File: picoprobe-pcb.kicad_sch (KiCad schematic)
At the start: 3 parts, among them J1 Conn_01x07_Male, J2 Conn_ARM_JTAG_SWD_10, U1 Pico

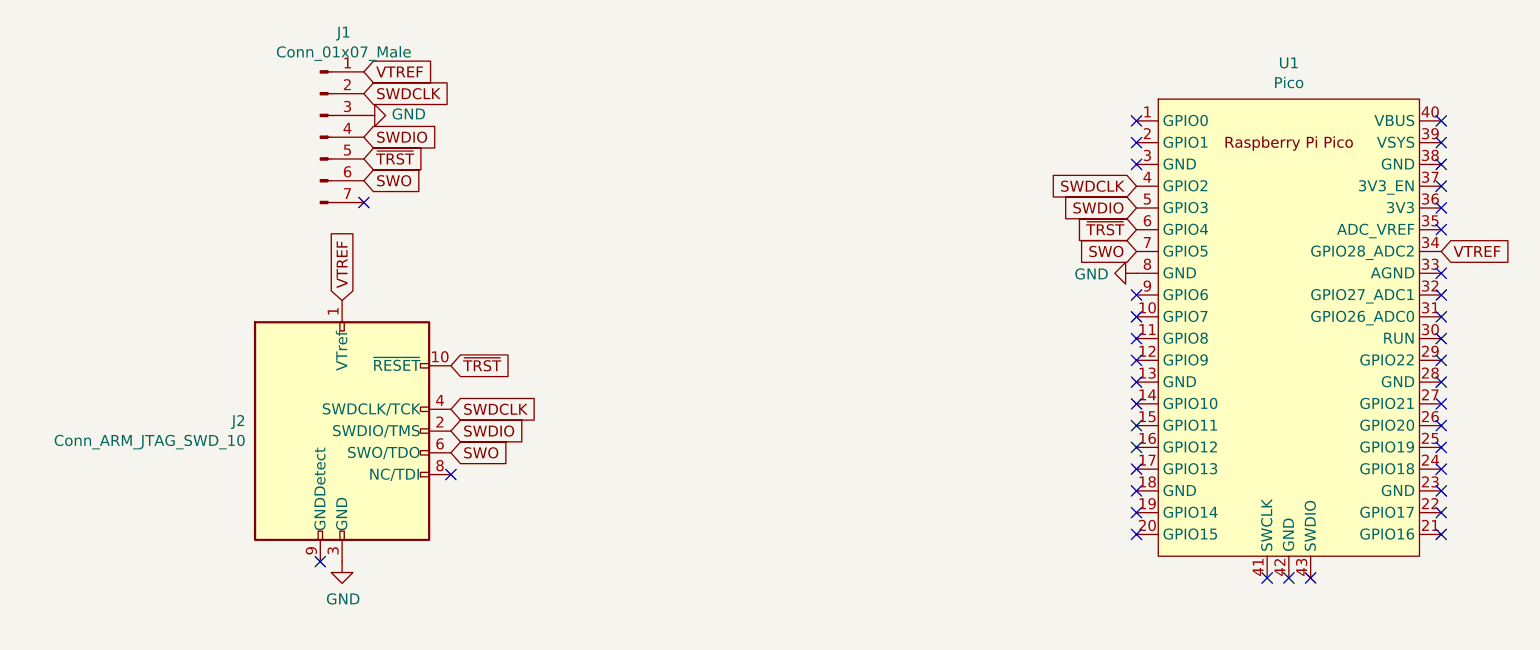
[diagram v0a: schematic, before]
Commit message: Clean up schematic
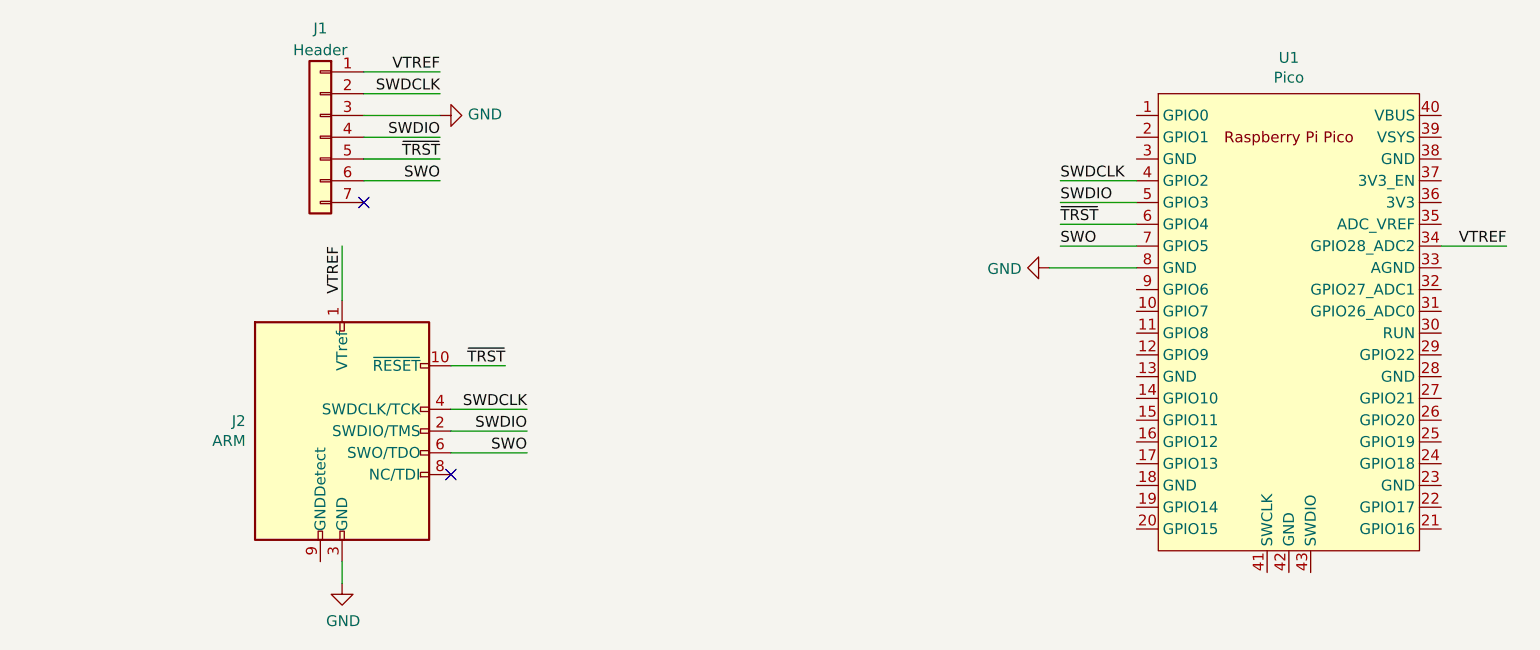
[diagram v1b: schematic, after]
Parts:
- J1: value Conn_01x07_Male -> Header; symbol picoprobe-pcb-rescue:Conn_01x07_Male-Connector -> Connector_Generic:Conn_01x07
- J2: value Conn_ARM_JTAG_SWD_10 -> ARM
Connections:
- no-connect marks 40 -> 2
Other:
- moved on the sheet: U1
